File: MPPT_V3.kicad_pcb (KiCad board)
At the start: 4 copper layers, 100 x 99.4 mm, 191 parts, among them CN1 XT60PW-M, CN2 XT60PW-M, J1 USB_C_Receptacle_USB2.0_16P, J2 Conn_01x05, SW1 SW_Push, SW2 SW_Push, SW3 SW_Push, SW4 SW_Push, SW5 SW_Push, SW6 SW_Push, U1 S130N10LF, U10 S130N10LF, U11 XJNG2103, U12 ADS1015IDGSR, U13 XJNG2103, U14 ESP32-S3(FN8), U15 TP181A1-CR, U16 XJNG2103, U17 XJNG2103, U18 INA240A2D, U19 W25Q128JVSIQTR, U2 S130N10LF, U20 ADS1015IDGSR, U21 INA240A2D, U22 S130N10LF, U23 S130N10LF, U24 LM2901, U3 S130N10LF, U4 S130N10LF, U5 LM5164DDAR, U6 AMS1117-3.3(XBLW), U7 LM5164DDAR, U8 TP181A1-CR, U9 S130N10LF, Y1 Crystal_GND24_Small

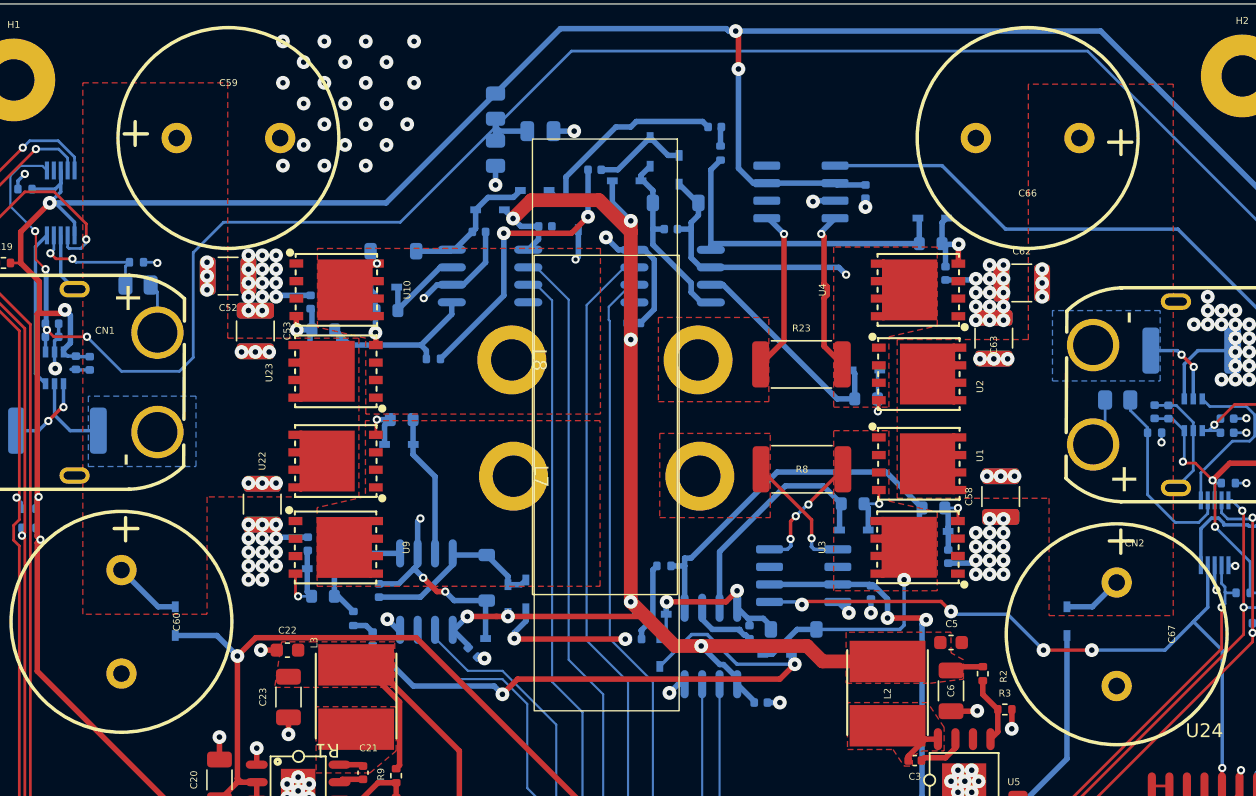
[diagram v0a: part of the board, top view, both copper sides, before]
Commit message: update before changing to currently used components
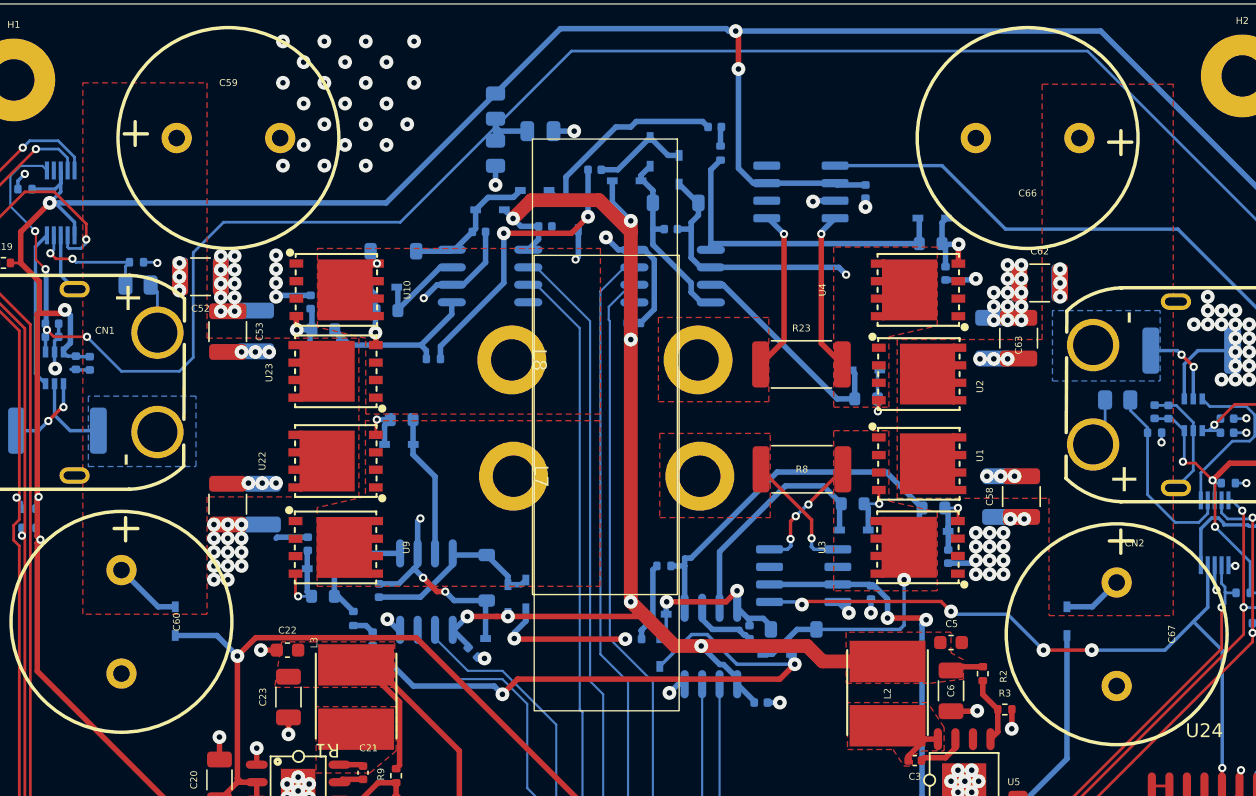
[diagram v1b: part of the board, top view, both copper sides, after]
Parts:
- moved C54 2.50 mm to (101.0, 89.5)
- moved C53 2.00 mm to (101.0, 77.0)
- moved C52 2.00 mm to (99.0, 73.0)
- moved C49 2.00 mm to (99.0, 73.0)
- moved C63 1.80 mm to (158.3, 77.5)
- moved C58 1.50 mm to (158.5, 89.0)
- moved C62 1.30 mm to (159.8, 73.5)
- moved C55 1.25 mm to (159.8, 73.5)
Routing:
- net /MCU/OUT_LO_PWMB: track 85.2 -> 84.3 mm

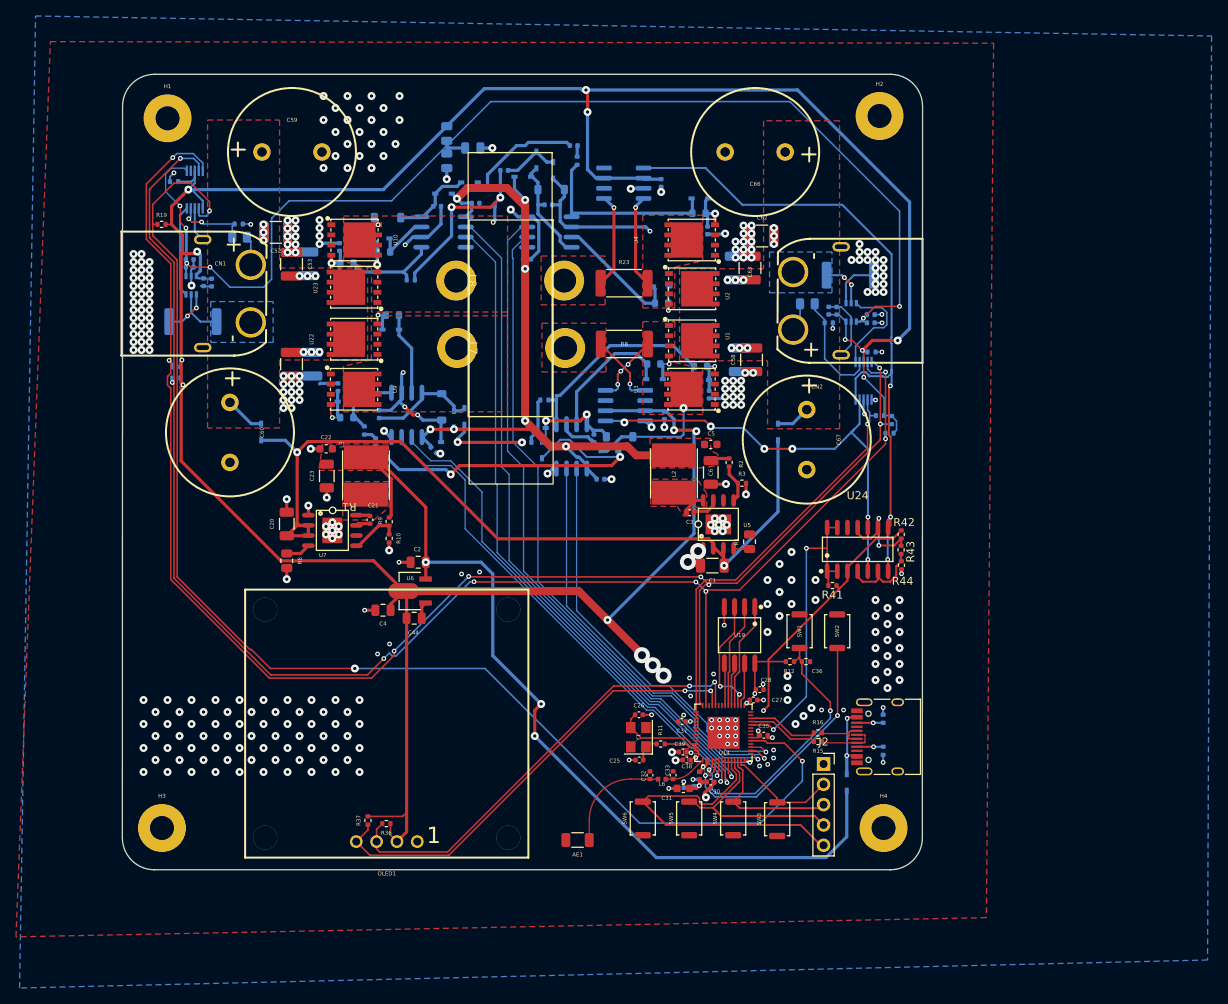
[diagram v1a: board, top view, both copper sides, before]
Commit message: latest version with PWM fan and thermistors for each FET bank
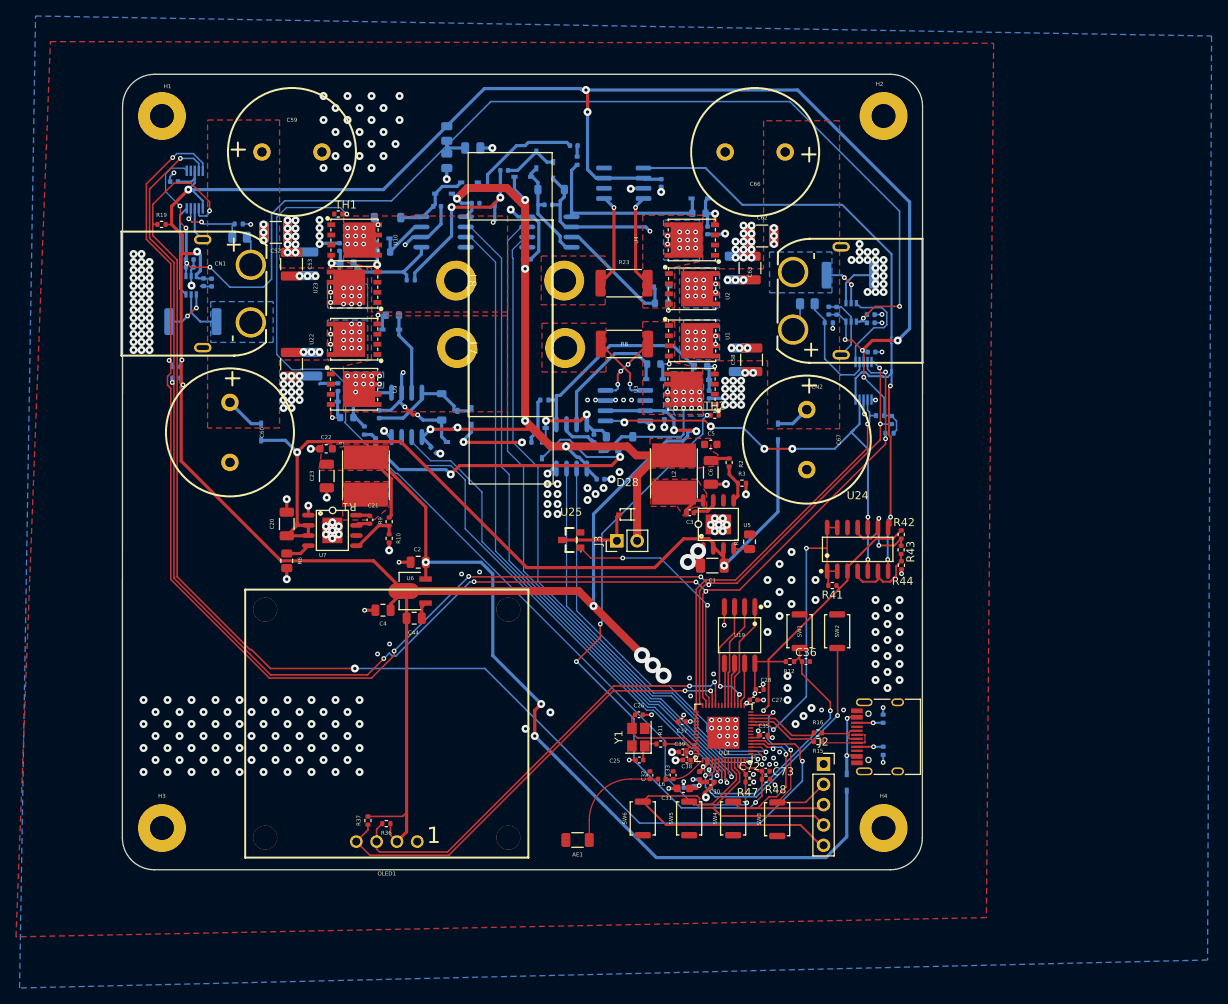
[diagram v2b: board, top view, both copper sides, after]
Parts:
- added C72: 1u, Capacitor_SMD:C_0402_1005Metric, F.Cu at (158.2, 140.8)
- added C73: 1u, Capacitor_SMD:C_0402_1005Metric, F.Cu at (160.3, 140.4)
- added D28: B16WS_C7420327, easyeda2kicad:SOD-323_L1.7-W1.3-LS2.5-FD, F.Cu at (143.0, 108.3)
- added J3: Fan_conn, Connector_PinHeader_2.54mm:PinHeader_1x02_P2.54mm_Vertical, F.Cu at (141.7, 111.6)
- added R47: 10k, Resistor_SMD:R_0402_1005Metric, F.Cu at (158.3, 141.8)
- added R48: 10k, Resistor_SMD:R_0402_1005Metric, F.Cu at (160.3, 141.4)
- added TH1: Thermistor_NTC, Resistor_SMD:R_0402_1005Metric, F.Cu at (106.8, 70.8)
- added TH2: Thermistor_NTC, Resistor_SMD:R_0402_1005Metric, F.Cu at (153.9, 95.9)
- added U25: AO3400_C4748804, footprint:SOT-23_L2.9-W1.3-P1.90-LS2.4-BR, F.Cu at (135.9, 111.5)
- C24, C36, C50: footprint Resistor_SMD:R_0402_1005Metric -> Capacitor_SMD:C_0402_1005Metric
- C34: value 10u -> 4.7u
- D1, D10, D11, D12, D13, D14, D15, D16, D17, D18, D2, D3, D4, D9: value B16WS_C7420327 -> B110WS
- R11: value R_Small -> 24nH
- R15, R16: value 10k -> 0
- R21, R22, R31, R32, R33, R38, R39, R40: value 4.2 -> 4.3
- R23, R8: value 1m -> 2m
- U11, U13, U16, U17: value XJNG2103 -> UCC27211DR
- Y1: footprint Crystal:Crystal_SMD_SeikoEpson_FA238V-4Pin_3.2x2.5mm -> Crystal:Crystal_SMD_SeikoEpson_FA238-4Pin_3.2x2.5mm
- moved D9 0.90 mm to (123.5, 96.1)
- moved D3 0.74 mm to (121.5, 99.2)
- moved D15 0.45 mm to (121.8, 96.4)
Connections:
- U14 pad 12: /MCU/IO_BTN2 -> /MCU/in_temp
- U14 pad 13: /MCU/IO_BTN1 -> /MCU/out_temp
- U14 pad 18: unconnected-(U14-GPIO13-Pad18) -> /MCU/IO_BTN2
- U14 pad 27: unconnected-(U14-GPIO21-Pad27) -> /MCU/IO_BTN1
- U14 pad 40: unconnected-(U14-GPIO35-Pad40) -> /MCU/FAN_PWM
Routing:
- net /MCU/in_temp: track 0.00 -> 121.2 mm, vias 0 -> 2
- net /MCU/out_temp: track 0.00 -> 79.2 mm, vias 0 -> 4
- net /MCU/FAN_PWM: track 0.00 -> 31.7 mm, vias 0 -> 2
- net +12V: track 95.1 -> 109.5 mm
- net +3.3V: track 459.4 -> 473.0 mm, vias 24 -> 26
- net Net-(D28-A): track 0.00 -> 10.8 mm
- net /MCU/IO_BTN2: track 17.2 -> 27.5 mm, vias 0 -> 2
- net /MCU/IO_BTN1: track 15.1 -> 25.0 mm, vias 0 -> 2
- net Net-(D1-K): track 102.2 -> 105.2 mm
- net /FETs/OUT_GATE_SW: track 29.7 -> 31.7 mm, vias 4 -> 17
- net Net-(D15-K): track 14.1 -> 15.0 mm
- net /MCU/ADC_READY2: track 164.4 -> 165.1 mm
- net Net-(D3-K): track 10.8 -> 10.1 mm
- net Net-(C25-Pad1): track 2.19 -> 2.86 mm
- net /FETs/IN_GATE_SW: track 15.8 -> 16.1 mm, vias 3 -> 13
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- added copper zone on B.Cu, net /FETs/IN_GATE_SW
- added copper zone on B.Cu, net /FETs/OUT_GATE_SW
- added copper zone on B.Cu, net /FETs1/IN_GATE_SW
- added copper zone on B.Cu, net /FETs1/OUT_GATE_SW
- added copper zone on B.Cu, net VDD
- added copper zone on B.Cu, net Vout

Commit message: production version v3
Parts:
- added J5: Fan_conn, Connector_PinHeader_2.54mm:PinHeader_1x02_P2.54mm_Vertical, F.Cu at (123.9, 150.5)
- added R50: 0, Resistor_SMD:R_0402_1005Metric, F.Cu at (126.3, 142.2)
- added R51: 0, Resistor_SMD:R_0402_1005Metric, F.Cu at (120.1, 142.1)
- added U27: SN65HVD234DR, footprint:SOIC-8_L4.9-W3.9-P1.27-LS6.0-BL, F.Cu at (123.1, 141.7)
- C53, C54, C58, C63: moved to B.Cu
- moved C51 11.4 mm to (100.0, 66.0), turned to 180 degrees
- moved C63 10.6 mm to (159.5, 67.0), turned to 0 degrees
- moved C66 6.04 mm to (164.9, 64.0), turned to 90 degrees
- moved C47 5.99 mm to (99.5, 94.0), turned to 180 degrees
- moved C59 5.89 mm to (95.2, 62.3), turned to 90 degrees
- moved C58 4.51 mm to (160.5, 93.0), turned to 0 degrees
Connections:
- U14 pad 49: unconnected-(U14-U0TXD-Pad49) -> /MCU/CAN_TX
- U14 pad 50: unconnected-(U14-U0RXD-Pad50) -> /MCU/CAN_RX
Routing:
- net /MCU/CAN_RX: track 0.00 -> 38.3 mm
- net /MCU/CAN_TX: track 0.00 -> 31.1 mm
- net +3.3V: track 473.0 -> 484.0 mm, vias 26 -> 28
- net /MCU/SDA_DISPL: track 58.2 -> 65.4 mm
- net /MCU/SCL_DISPL: track 57.7 -> 64.3 mm
- net Net-(J5-Pin_2): track 0.00 -> 6.46 mm
- net Net-(J5-Pin_1): track 0.00 -> 6.30 mm
- net GND: track 106.4 -> 111.0 mm, vias 349 -> 358
- net Net-(U27-EN): track 0.00 -> 2.40 mm
- net /FETs/OUT_GATE_SW: track 31.7 -> 29.3 mm, vias 17 -> 4
- net Net-(U27-RS): track 0.00 -> 2.31 mm
- net Vout: vias 31 -> 15
- net VDD: vias 33 -> 15
- net /FETs1/OUT_GATE_SW: vias 13 -> 2
- net /FETs1/IN_GATE_SW: vias 12 -> 3
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- removed copper zone on B.Cu, net /FETs/OUT_GATE_SW
- removed copper zone on B.Cu, net /FETs1/IN_GATE_SW
- removed copper zone on B.Cu, net /FETs1/OUT_GATE_SW
- removed copper zone on B.Cu, net VDD
- removed copper zone on B.Cu, net Vout
